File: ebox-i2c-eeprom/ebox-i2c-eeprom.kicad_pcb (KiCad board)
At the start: 2 copper layers, 45 x 75 mm, 11 parts, among them J1 xconch_pinheader_2x40, J2 xconch_pinsocket_2x40, U1 AT24CS64-SSHM

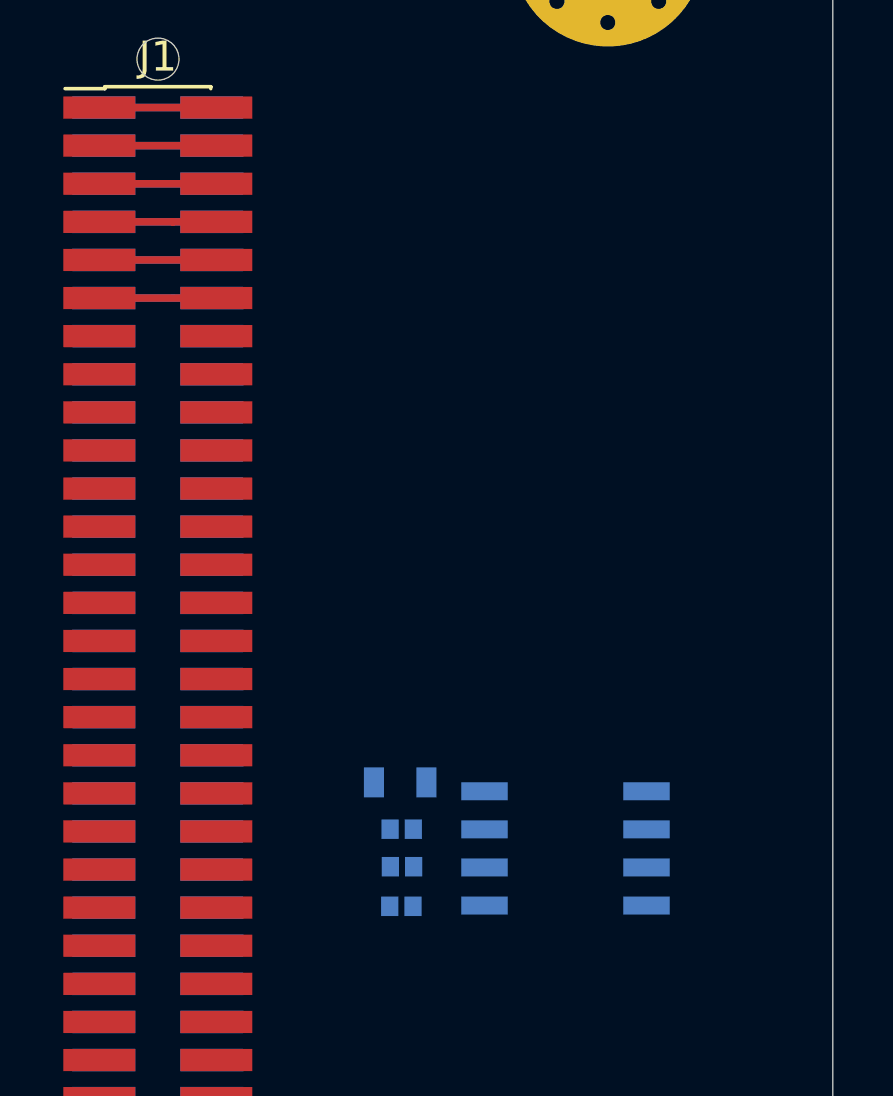
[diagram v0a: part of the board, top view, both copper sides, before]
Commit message: [ebox]add ebox-i2c eeprom
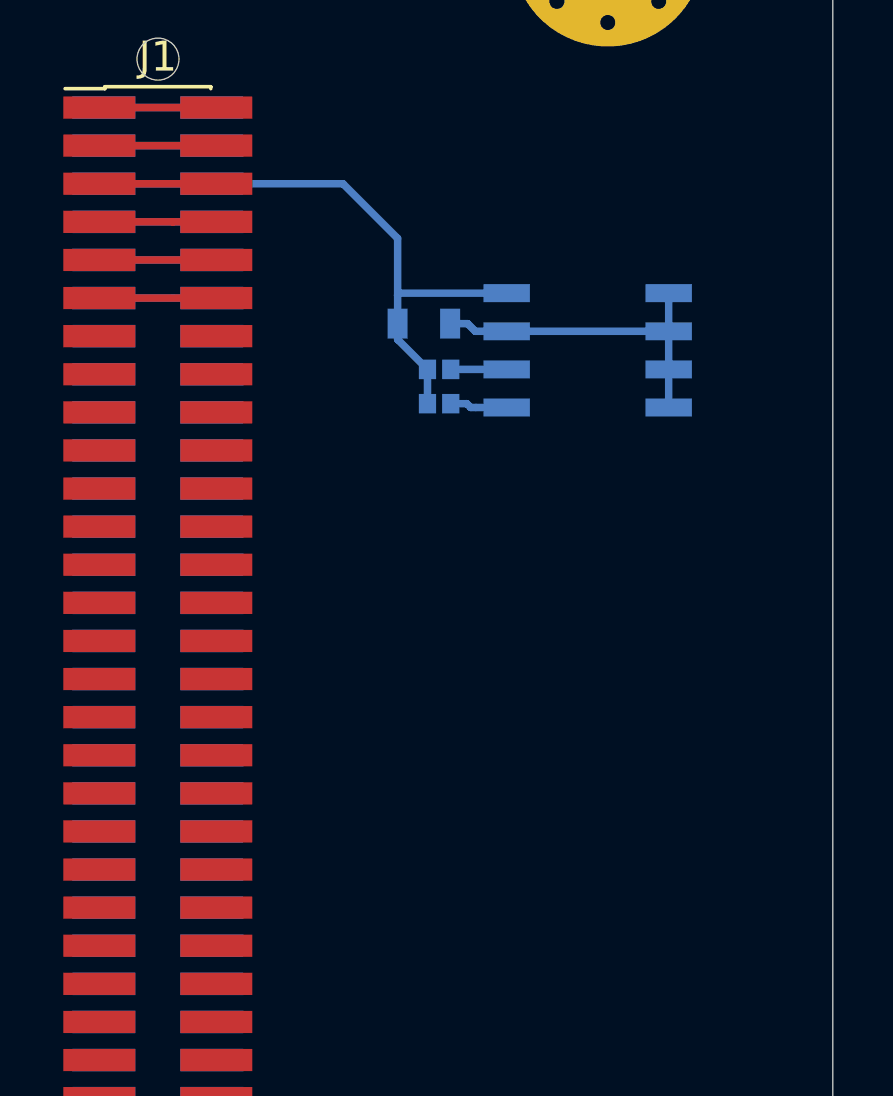
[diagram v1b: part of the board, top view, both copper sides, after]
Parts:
- removed R3: 4.7K, Resistor_SMD:R_0402_1005Metric
- J1: footprint Connector_PinHeader_1.27mm:PinHeader_2x40_P1.27mm_Vertical_SMD -> xconch:xconch_pinheader_2x40
- moved R1 16.8 mm to (31.9, 22.6)
- moved R2 16.6 mm to (31.9, 21.5)
- moved U1 16.6 mm to (36.8, 20.8)
- moved C1 15.3 mm to (31.4, 19.9)
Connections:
- U1 pad 7: Net-(R3-Pad2) -> GND
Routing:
- net +3V3: track 7.50 -> 24.0 mm
- net GND: track 7.50 -> 18.7 mm
- net /I2C_SDA: track 0.00 -> 1.92 mm
- net /I2C_SCL: track 0.00 -> 1.87 mm

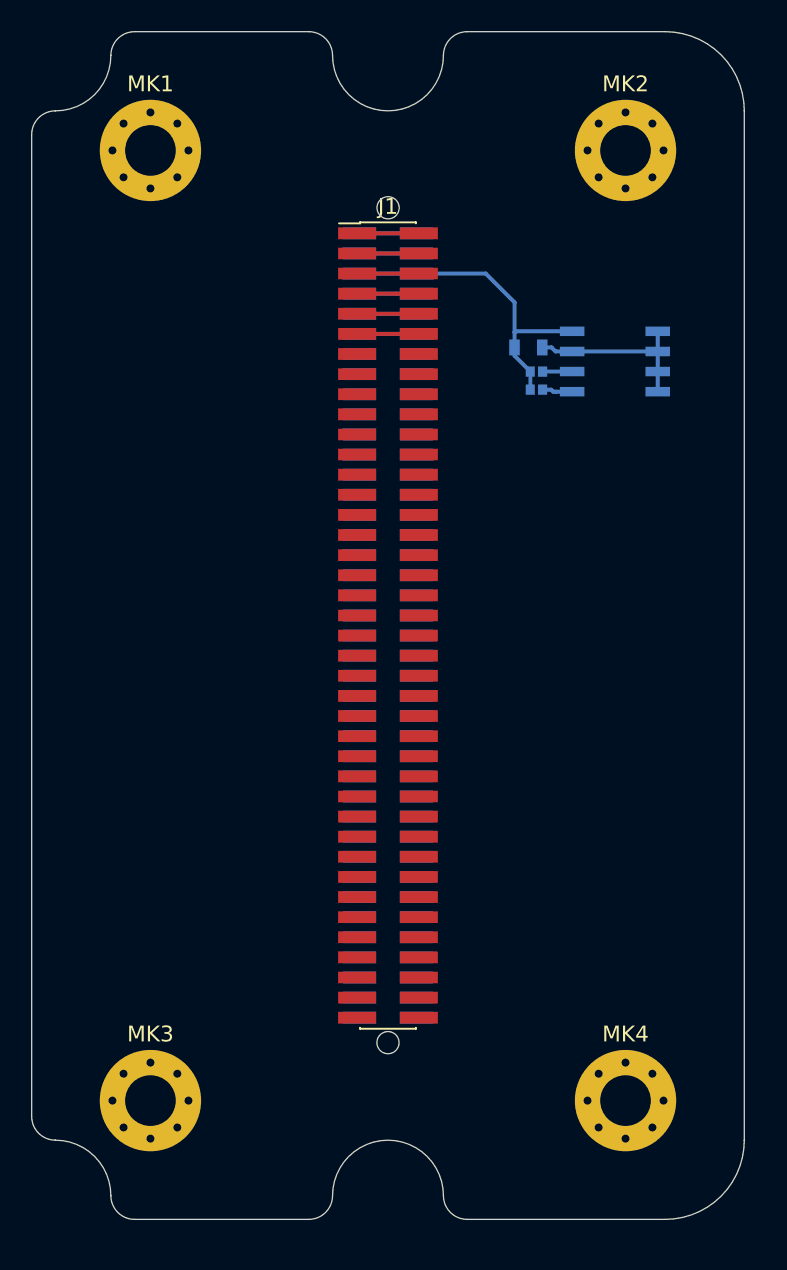
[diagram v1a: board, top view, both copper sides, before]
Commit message: working on ebox i2c eeprom
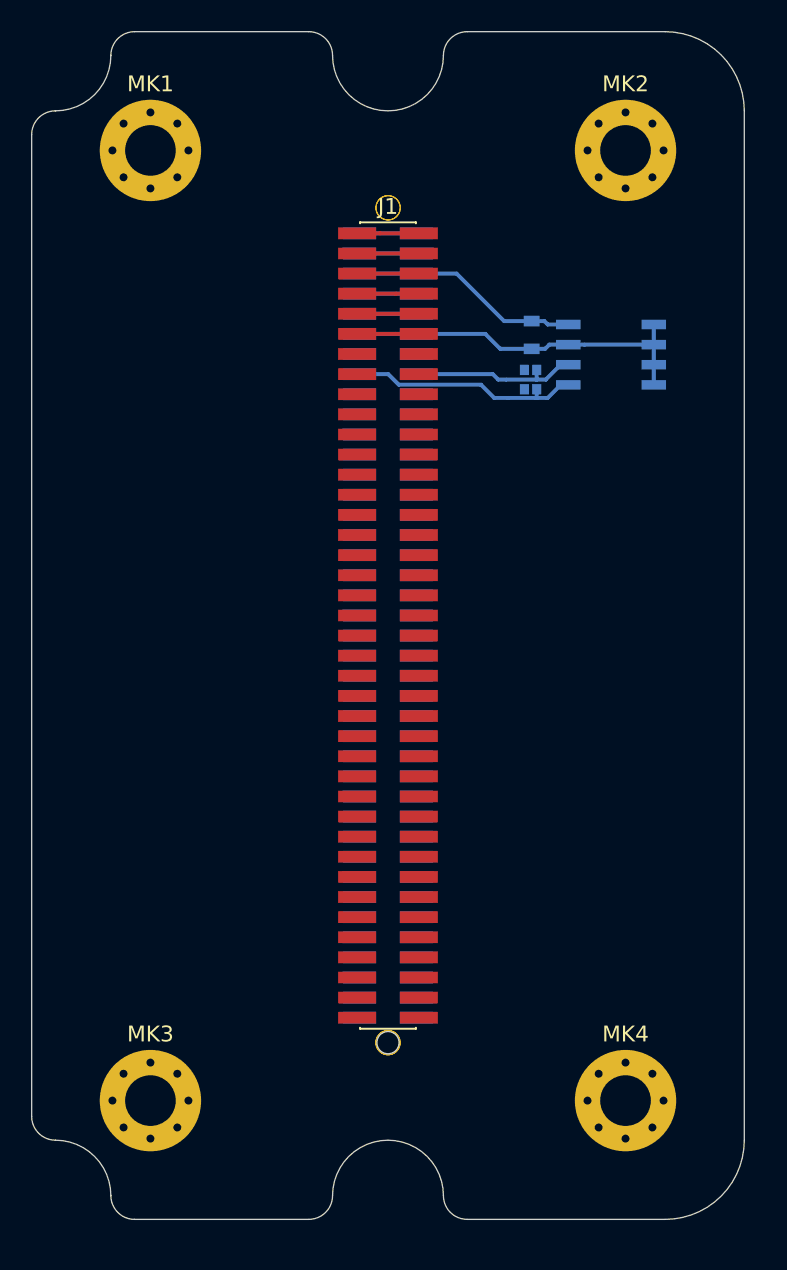
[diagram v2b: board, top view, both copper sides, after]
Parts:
- U1: value AT24CS64-SSHM -> AT24C64
- moved C1 0.81 mm to (31.6, 19.2), turned to 270 degrees
- moved U1 0.50 mm to (36.6, 20.4)
- moved R2 0.39 mm to (31.5, 21.4)
- moved R1 0.38 mm to (31.5, 22.6)
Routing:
- net /I2C_SDA: track 1.92 -> 14.7 mm
- net /I2C_SCL: track 1.87 -> 10.7 mm
- net GND: track 18.7 -> 26.8 mm
- net +3V3: track 24.0 -> 18.4 mm
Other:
- outline, holes or cut-outs redrawn
- net class Default: clearance 0.2 -> 0.1
- rule trace_clearance: 0.2 -> 0.1
- rule trace_min: 0.2 -> 0.1

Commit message: update some documents
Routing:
- net +3V3: track 18.4 -> 41.1 mm, vias 0 -> 5
- net /PWM1: track 0.00 -> 3.06 mm, vias 0 -> 1
- net /NC7: track 0.00 -> 3.06 mm, vias 0 -> 1
- net /NC3: track 0.00 -> 3.06 mm, vias 0 -> 1
- net /NC29: track 0.00 -> 3.06 mm, vias 0 -> 1
- net /NC11: track 0.00 -> 3.06 mm, vias 0 -> 1
- net /GPIO9: track 0.00 -> 3.06 mm, vias 0 -> 1
- net /GPIO7: track 0.00 -> 3.06 mm, vias 0 -> 1
- net /GPIO3: track 0.00 -> 3.06 mm, vias 0 -> 1
- net /DAC1: track 0.00 -> 3.06 mm, vias 0 -> 1
- net /UART_RX: track 0.00 -> 3.06 mm, vias 0 -> 1
- net /SPI_CS: track 0.00 -> 3.06 mm, vias 0 -> 1
- net /SPI_CLK: track 0.00 -> 3.06 mm, vias 0 -> 1
- net /SDIO_D1: track 0.00 -> 3.06 mm, vias 0 -> 1
- net /I2S_LRCLK: track 0.00 -> 3.06 mm, vias 0 -> 1
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- added copper zone on B.Cu, net GND
- added copper zone on F.Cu, net GND
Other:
- rule via_min_drill: 0.3 -> 0.1
- rule via_min_size: 0.4 -> 0.1
- board text added: "EBOX - I2C EEPROM"
- board text added: "I2C_SCL"
- board text added: "I2C_SDA"
- board text added: "PIN"

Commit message: update some documents
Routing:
- net GND: track 26.8 -> 35.9 mm, vias 0 -> 35
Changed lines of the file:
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@@
     (thickness 1.6)
     (drawings 34)
-    (tracks 384)
+    (tracks 422)
     (zones 0)
     (modules 10)
@@
     (36 B.SilkS user)
     (37 F.SilkS user)
-    (38 B.Mask user)
+    (38 B.Mask user hide)
     (39 F.Mask user)
     (40 Dwgs.User user)
@@
   )
   (setup
-    (last_trace_width 0.5)
+    (last_trace_width 0.25)
     (user_trace_width 0.125)
     (user_trace_width 0.25)
@@
       (outputformat 1)
       (mirror false)
-      (drillshape 1)
+      (drillshape 0)
       (scaleselection 1)
-      (outputdirectory ""))
+      (outputdirectory gerber))
   )
   (net 0 "")
@@
       (effects (font (size 1 1) (thickness 0.15)) (justify mirror))
     )
-    (fp_text value 4.7K (at 0 -1.5) (layer B.Fab)
+    (fp_text value 4.7K (at -3.5622 0.1524) (layer B.Fab)
       (effects (font (size 1 1) (thickness 0.15)) (justify mirror))
     )
@@
     (fp_line (start 0.82 0.48) (end 0.82 -0.48) (layer B.CrtYd) (width 0.05))
     (fp_line (start 0.82 -0.48) (end -0.82 -0.48) (layer B.CrtYd) (width 0.05))
-    (fp_text user %R (at 0 0.88) (layer B.Fab)
+    (fp_text user %R (at -1.2762 0.0889) (layer B.Fab)
       (effects (font (size 0.5 0.5) (thickness 0.08)) (justify mirror))
     )
@@
       (effects (font (size 1 1) (thickness 0.15)) (justify mirror))
     )
-    (fp_text value 4.7K (at 0 -1.5) (layer B.Fab)
+    (fp_text value 4.7K (at -3.5622 0.0381) (layer B.Fab)
       (effects (font (size 1 1) (thickness 0.15)) (justify mirror))
     )
@@
     (fp_line (start 0.82 0.48) (end 0.82 -0.48) (layer B.CrtYd) (width 0.05))
     (fp_line (start 0.82 -0.48) (end -0.82 -0.48) (layer B.CrtYd) (width 0.05))
-    (fp_text user %R (at 0 0.88) (layer B.Fab)
+    (fp_text user %R (at -1.2762 0.1016) (layer B.Fab)
       (effects (font (size 0.5 0.5) (thickness 0.08)) (justify mirror))
     )
@@
       (effects (font (size 1 1) (thickness 0.15)) (justify mirror))
     )
-    (fp_text value 0.1uF (at 0 -1.65 270) (layer B.Fab)
+    (fp_text value 0.1uF (at 0.1524 2.8067 180) (layer B.Fab)
       (effects (font (size 1 1) (thickness 0.15)) (justify mirror))
     )
@@
     )
   )
+  (gr_circle (center 22.500537 63.84) (end 21.800537 63.84) (layer Edge.Cuts) (width 0))
   (gr_text PIN (at 31.327678 38.448295 90) (layer F.SilkS)
     (effects (font (size 1.5 1.5) (thickness 0.3)))
@@
     (effects (font (size 1.5 1.5) (thickness 0.3)))
   )
-  (gr_circle (center 22.500537 63.84) (end 21.800537 63.84) (layer Edge.Cuts) (width 0))
   (gr_line (start 27.5 0) (end 40 0) (layer Edge.Cuts) (width 0))
   (gr_arc (start 27.5 1.5) (end 27.5 0) (angle -90) (layer Edge.Cuts) (width 0))
@@
   (segment (start 20.55 17.815) (end 24.45 17.815) (width 0.5) (layer F.Cu) (net 4))
   (segment (start 20.7 17.815) (end 24.3 17.815) (width 0.5) (layer B.Cu) (net 4))
+  (segment (start 20.7 19.085) (end 17.815 19.085) (width 0.5) (layer B.Cu) (net 73))
+  (segment (start 24.45 19.085) (end 27.905 19.085) (width 0.5) (layer F.Cu) (net 73))
+  (segment (start 20.55 19.085) (end 17.815 19.085) (width 0.5) (layer F.Cu) (net 73))
+  (via (at 31.75 59.69) (size 0.2) (drill 0.1) (layers F.Cu B.Cu) (net 73))
+  (via (at 31.75 50.8) (size 0.2) (drill 0.1) (layers F.Cu B.Cu) (net 73))
+  (via (at 31.75 39.37) (size 0.2) (drill 0.1) (layers F.Cu B.Cu) (net 73))
+  (via (at 31.75 27.94) (size 0.2) (drill 0.1) (layers F.Cu B.Cu) (net 73))
+  (via (at 36.83 59.69) (size 0.2) (drill 0.1) (layers F.Cu B.Cu) (net 73))
+  (via (at 36.83 50.8) (size 0.2) (drill 0.1) (layers F.Cu B.Cu) (net 73))
+  (via (at 36.83 39.37) (size 0.2) (drill 0.1) (layers F.Cu B.Cu) (net 73))
+  (via (at 36.83 27.94) (size 0.2) (drill 0.1) (layers F.Cu B.Cu) (net 73))
+  (via (at 36.83 20.32) (size 0.2) (drill 0.1) (layers F.Cu B.Cu) (net 73))
+  (via (at 41.91 59.69) (size 0.2) (drill 0.1) (layers F.Cu B.Cu) (net 73))
+  (via (at 41.91 50.8) (size 0.2) (drill 0.1) (layers F.Cu B.Cu) (net 73))
+  (via (at 41.91 39.37) (size 0.2) (drill 0.1) (layers F.Cu B.Cu) (net 73))
+  (via (at 41.91 27.94) (size 0.2) (drill 0.1) (layers F.Cu B.Cu) (net 73))
+  (via (at 41.91 20.32) (size 0.2) (drill 0.1) (layers F.Cu B.Cu) (net 73))
+  (via (at 31.75 12.7) (size 0.2) (drill 0.1) (layers F.Cu B.Cu) (net 73))
+  (via (at 36.83 12.7) (size 0.2) (drill 0.1) (layers F.Cu B.Cu) (net 73))
+  (via (at 41.91 12.7) (size 0.2) (drill 0.1) (layers F.Cu B.Cu) (net 73))
+  (via (at 13.97 59.69) (size 0.2) (drill 0.1) (layers F.Cu B.Cu) (net 73))
+  (via (at 13.97 49.53) (size 0.2) (drill 0.1) (layers F.Cu B.Cu) (net 73))
+  (via (at 13.97 39.37) (size 0.2) (drill 0.1) (layers F.Cu B.Cu) (net 73))
+  (via (at 13.97 27.94) (size 0.2) (drill 0.1) (layers F.Cu B.Cu) (net 73))
+  (via (at 13.97 20.32) (size 0.2) (drill 0.1) (layers F.Cu B.Cu) (net 73))
+  (via (at 13.97 12.7) (size 0.2) (drill 0.1) (layers F.Cu B.Cu) (net 73))
+  (via (at 8.89 12.7) (size 0.2) (drill 0.1) (layers F.Cu B.Cu) (net 73))
+  (via (at 8.89 20.32) (size 0.2) (drill 0.1) (layers F.Cu B.Cu) (net 73))
+  (via (at 8.89 27.94) (size 0.2) (drill 0.1) (layers F.Cu B.Cu) (net 73))
+  (via (at 8.89 39.37) (size 0.2) (drill 0.1) (layers F.Cu B.Cu) (net 73))
+  (via (at 8.89 49.53) (size 0.2) (drill 0.1) (layers F.Cu B.Cu) (net 73))
+  (via (at 8.89 59.69) (size 0.2) (drill 0.1) (layers F.Cu B.Cu) (net 73))
+  (via (at 3.81 59.69) (size 0.2) (drill 0.1) (layers F.Cu B.Cu) (net 73))
+  (via (at 3.81 49.53) (size 0.2) (drill 0.1) (layers F.Cu B.Cu) (net 73))
+  (via (at 3.81 39.37) (size 0.2) (drill 0.1) (layers F.Cu B.Cu) (net 73))
+  (via (at 3.81 27.94) (size 0.2) (drill 0.1) (layers F.Cu B.Cu) (net 73))
+  (via (at 3.81 20.32) (size 0.2) (drill 0.1) (layers F.Cu B.Cu) (net 73))
+  (via (at 3.81 12.7) (size 0.2) (drill 0.1) (layers F.Cu B.Cu) (net 73))
   (segment (start 39.2836 18.4912) (end 39.2836 22.3012) (width 0.5) (layer B.Cu) (net 73))
   (segment (start 33.8836 19.7612) (end 39.2836 19.7612) (width 0.5) (layer B.Cu) (net 73))

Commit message: update some documents
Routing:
- net GND: track 35.9 -> 165.5 mm
- net +3V3: track 41.1 -> 31.8 mm
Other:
- board text removed: "I2C_SCL"
- board text removed: "I2C_SDA"
- board text removed: "PIN"
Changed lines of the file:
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@@
   (general
     (thickness 1.6)
-    (drawings 34)
-    (tracks 422)
+    (drawings 22)
+    (tracks 425)
     (zones 0)
     (modules 10)
@@
   )
   (gr_circle (center 22.500537 63.84) (end 21.800537 63.84) (layer Edge.Cuts) (width 0))
-  (gr_text PIN (at 31.327678 38.448295 90) (layer F.SilkS)
-    (effects (font (size 1.5 1.5) (thickness 0.3)))
-  )
-  (gr_line (start 30.057678 33.368295) (end 32.597678 33.368295) (layer F.SilkS) (width 0.2))
-  (gr_line (start 30.057678 43.528295) (end 30.057678 33.368295) (layer F.SilkS) (width 0.2))
-  (gr_line (start 32.597678 43.528295) (end 30.057678 43.528295) (layer F.SilkS) (width 0.2))
-  (gr_line (start 35.137678 43.528295) (end 35.137678 33.368295) (layer F.SilkS) (width 0.2))
-  (gr_line (start 32.597678 43.528295) (end 35.137678 43.528295) (layer F.SilkS) (width 0.2))
-  (gr_line (start 32.597678 33.368295) (end 32.597678 43.528295) (layer F.SilkS) (width 0.2))
-  (gr_line (start 37.677678 33.368295) (end 32.597678 33.368295) (layer F.SilkS) (width 0.2))
-  (gr_line (start 37.677678 43.528295) (end 37.677678 33.368295) (layer F.SilkS) (width 0.2))
-  (gr_line (start 32.597678 43.528295) (end 37.677678 43.528295) (layer F.SilkS) (width 0.2))
-  (gr_text I2C_SCL (at 36.407678 38.448295 90) (layer F.SilkS)
-    (effects (font (size 1.5 1.5) (thickness 0.3)))
-  )
-  (gr_text I2C_SDA (at 33.867678 38.448295 90) (layer F.SilkS)
-    (effects (font (size 1.5 1.5) (thickness 0.3)))
-  )
-  (gr_text "EBOX - I2C EEPROM" (at 40.64 38.1 90) (layer F.SilkS)
+  (gr_text "EBOX - I2C EEPROM" (at 15.875 36.83 90) (layer F.SilkS)
     (effects (font (size 1.5 1.5) (thickness 0.3)))
   )
@@
   (segment (start 20.55 17.815) (end 24.45 17.815) (width 0.5) (layer F.Cu) (net 4))
   (segment (start 20.7 17.815) (end 24.3 17.815) (width 0.5) (layer B.Cu) (net 4))
+  (segment (start 7.5 19.05) (end 7.5 7.5) (width 0.5) (layer F.Cu) (net 73))
+  (segment (start 7.5 67.5) (end 7.5 19.05) (width 0.5) (layer F.Cu) (net 73))
+  (segment (start 20.55 19.085) (end 7.535 19.085) (width 0.5) (layer F.Cu) (net 73))
+  (segment (start 7.535 19.085) (end 7.5 19.05) (width 0.5) (layer F.Cu) (net 73))
+  (segment (start 7.5 67.5) (end 12.025483 67.5) (width 0.5) (layer F.Cu) (net 73))
+  (segment (start 12.025483 67.5) (end 37.5 67.5) (width 0.5) (layer F.Cu) (net 73))
+  (segment (start 7.5 7.5) (end 37.5 7.5) (width 0.5) (layer F.Cu) (net 73))
   (segment (start 20.7 19.085) (end 17.815 19.085) (width 0.5) (layer B.Cu) (net 73))
-  (segment (start 24.45 19.085) (end 27.905 19.085) (width 0.5) (layer F.Cu) (net 73))
   (segment (start 20.55 19.085) (end 17.815 19.085) (width 0.5) (layer F.Cu) (net 73))
   (via (at 31.75 59.69) (size 0.2) (drill 0.1) (layers F.Cu B.Cu) (net 73))
@@
   (segment (start 24.45 19.085) (end 20.55 19.085) (width 0.5) (layer F.Cu) (net 73))
   (segment (start 24.3 19.085) (end 20.7 19.085) (width 0.5) (layer B.Cu) (net 73))
-  (segment (start 24.45 15.275) (end 26.959 15.275) (width 0.5) (layer F.Cu) (net 74))
-  (segment (start 26.959 15.275) (end 29.972 18.288) (width 0.5) (layer F.Cu) (net 74))
+  (segment (start 24.3 15.275) (end 26.959 15.275) (width 0.5) (layer B.Cu) (net 74))
+  (segment (start 26.959 15.275) (end 29.972 18.288) (width 0.5) (layer B.Cu) (net 74))
   (segment (start 29.972 22.606) (end 29.972 18.288) (width 0.5) (layer F.Cu) (net 74))
   (segment (start 31.1147 22.5806) (end 29.9974 22.5806) (width 0.5) (layer B.Cu) (net 74))
@@
   (segment (start 29.972 18.288) (end 32.385 18.288) (width 0.5) (layer B.Cu) (net 74))
   (segment (start 32.385 18.288) (end 32.5882 18.4912) (width 0.5) (layer B.Cu) (net 74))
-  (segment (start 24.3 15.275) (end 26.959 15.275) (width 0.5) (layer B.Cu) (net 74))
-  (segment (start 26.959 15.275) (end 29.972 18.288) (width 0.5) (layer B.Cu) (net 74))
   (segment (start 20.55 15.275) (end 24.45 15.275) (width 0.5) (layer F.Cu) (net 74))
   (segment (start 20.7 15.275) (end 24.3 15.275) (width 0.5) (layer B.Cu) (net 74))
@@
   (segment (start 32.4688 21.971) (end 33.4086 21.0312) (width 0.25) (layer B.Cu) (net 8))
   (segment (start 33.4086 21.0312) (end 33.8836 21.0312) (width 0.25) (layer B.Cu) (net 8))
-  (segment (start 24.3 15.275) (end 26.832 15.275) (width 0.25) (layer B.Cu) (net 74))
   (segment (start 32.3736 18.2766) (end 32.5882 18.4912) (width 0.25) (layer B.Cu) (net 74))
   (segment (start 31.5722 18.2766) (end 32.3736 18.2766) (width 0.25) (layer B.Cu) (net 74))
@@
     (polygon
       (pts
-        (xy 0 0) (xy 0 76.2) (xy 45.72 76.2) (xy 45.72 0)
+        (xy 0 0) (xy 0 75.565) (xy 45.085 75.565) (xy 45.085 0)
       )
     )
@@
     (polygon
       (pts
-        (xy 0 0) (xy 0 76.2) (xy 45.72 76.2) (xy 45.72 0)
+        (xy 0 0) (xy 0 75.565) (xy 45.085 75.565) (xy 45.085 0)
       )
     )

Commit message: update ebox
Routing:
- net /I2C_SDA: track 14.7 -> 16.2 mm
